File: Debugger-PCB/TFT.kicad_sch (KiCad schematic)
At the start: 7 parts, among them U6 XPT2046TS

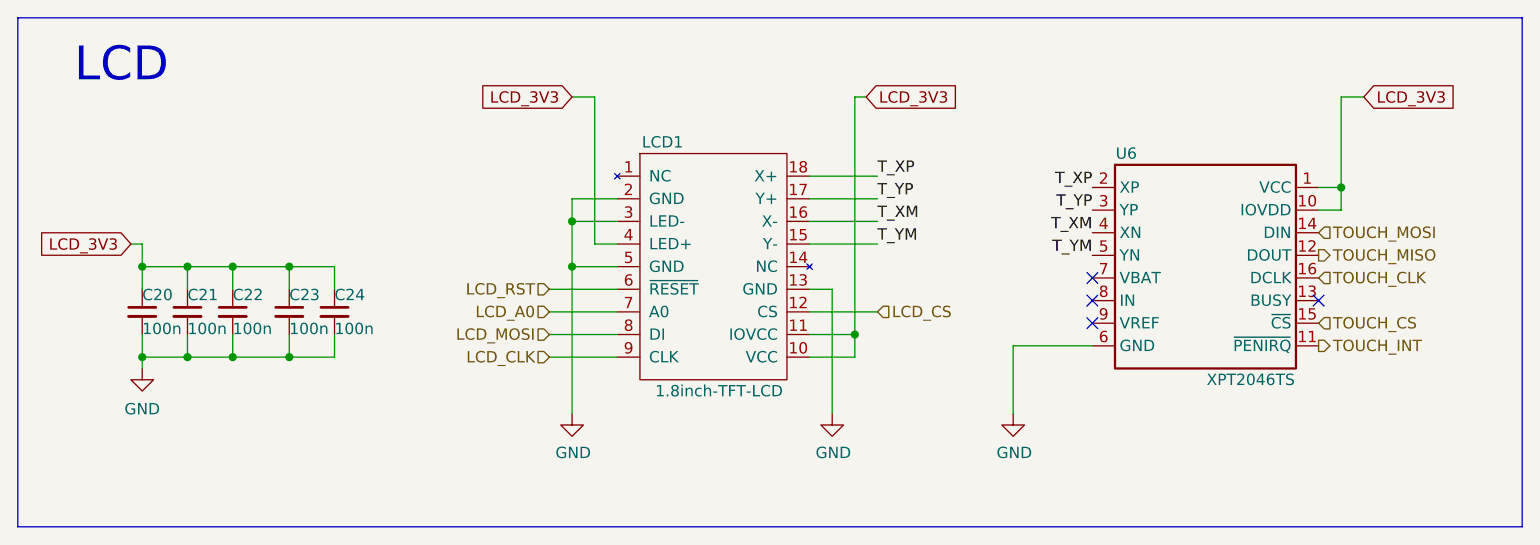
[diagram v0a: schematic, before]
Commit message: fix some details of PCB
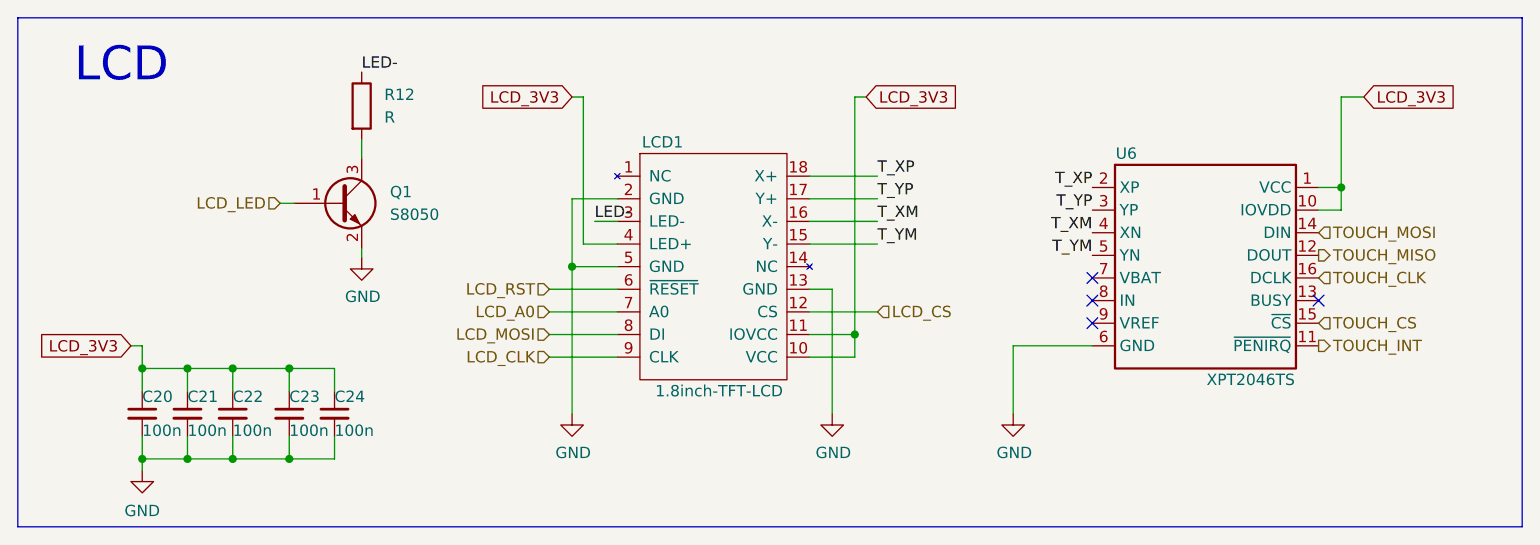
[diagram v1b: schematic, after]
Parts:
- added Q1: S8050, Package_TO_SOT_SMD:SOT-23, symbol Periph:S8050
- added R12: R, GENERAL_RCL_SMD:L0603(1608M), symbol Device:R
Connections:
- net GND: now also Q1.2 (E); no longer LCD1.3 (LED-)
- new net: Q1.3 (C), R12.2
- new net LCD_LED: Q1.1 (B)
- new net LED-: LCD1.3 (LED-), R12.1
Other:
- moved on the sheet: C20, C21, C22, C23, C24

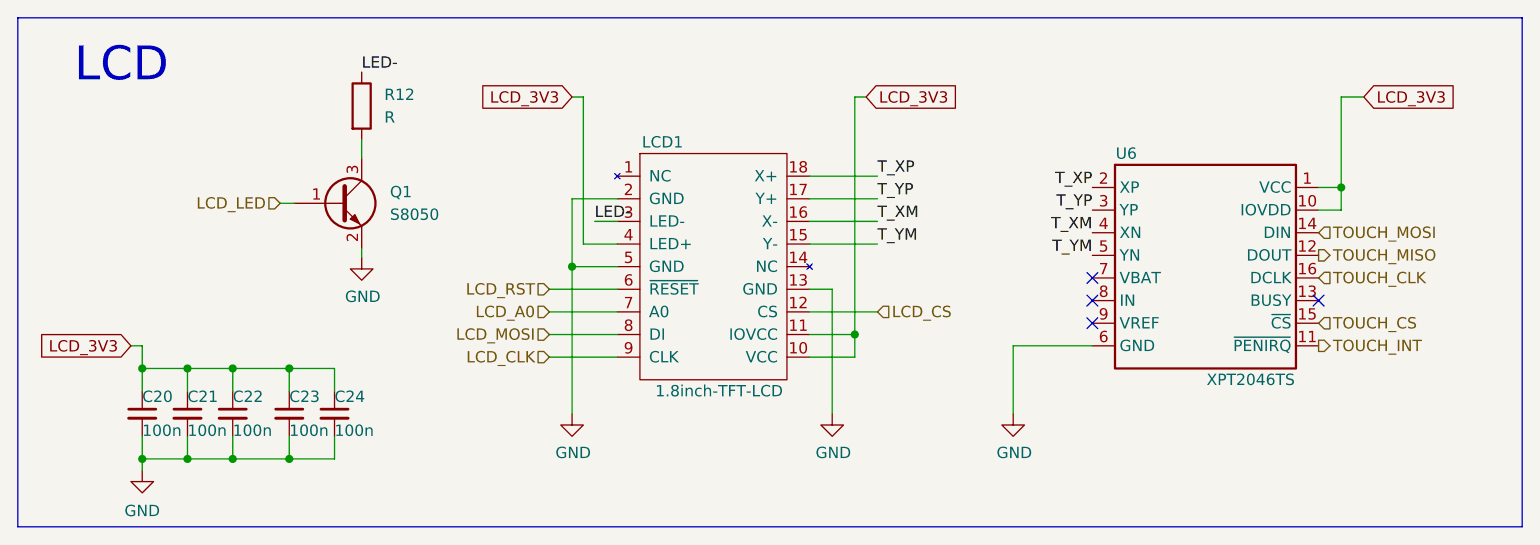
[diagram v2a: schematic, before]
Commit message: change the file name debugger-code into debugger_code_f103. Change the stm32f103rct6 into stm32f407vet6. Add file debugger_code_f407
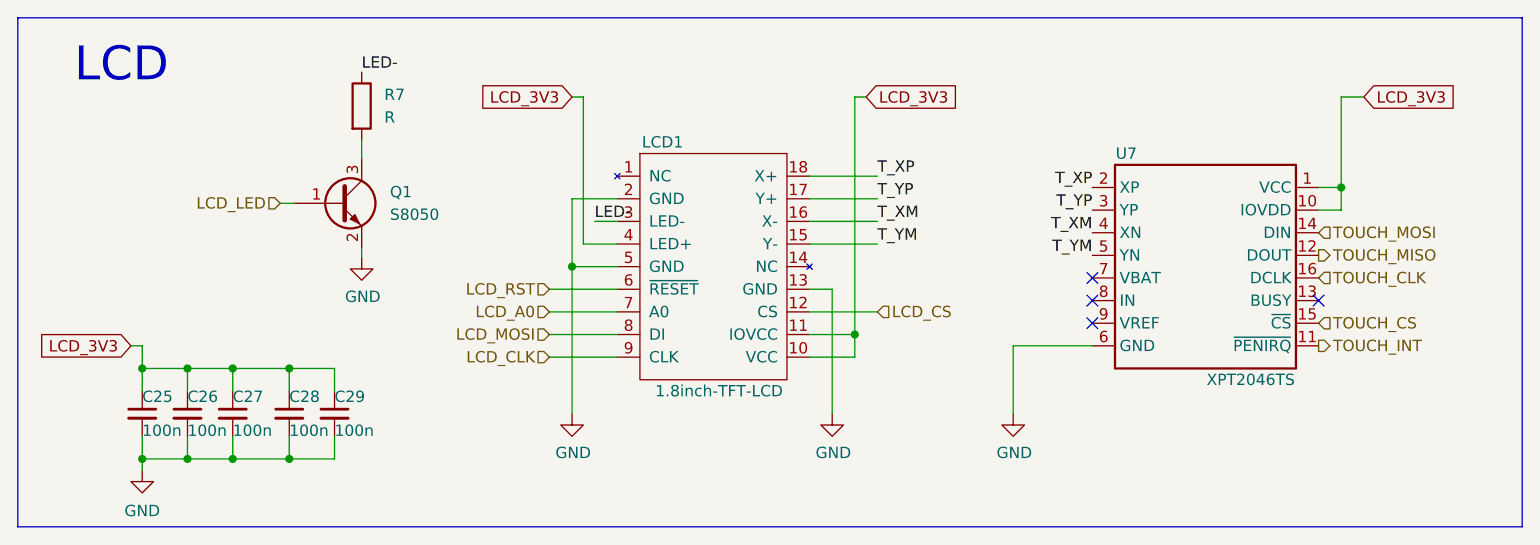
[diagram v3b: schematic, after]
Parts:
- R7: renamed from R12; footprint GENERAL_RCL_SMD:L0603(1608M) -> Resistor_SMD:R_0603_1608Metric
- renumbered C20 to C25, C21 to C26, C22 to C27, C23 to C28, C24 to C29, U6 to U7
